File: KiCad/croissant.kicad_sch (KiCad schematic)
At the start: 7 parts, among them J1 USB_C_Receptacle, U1 LMC555xM

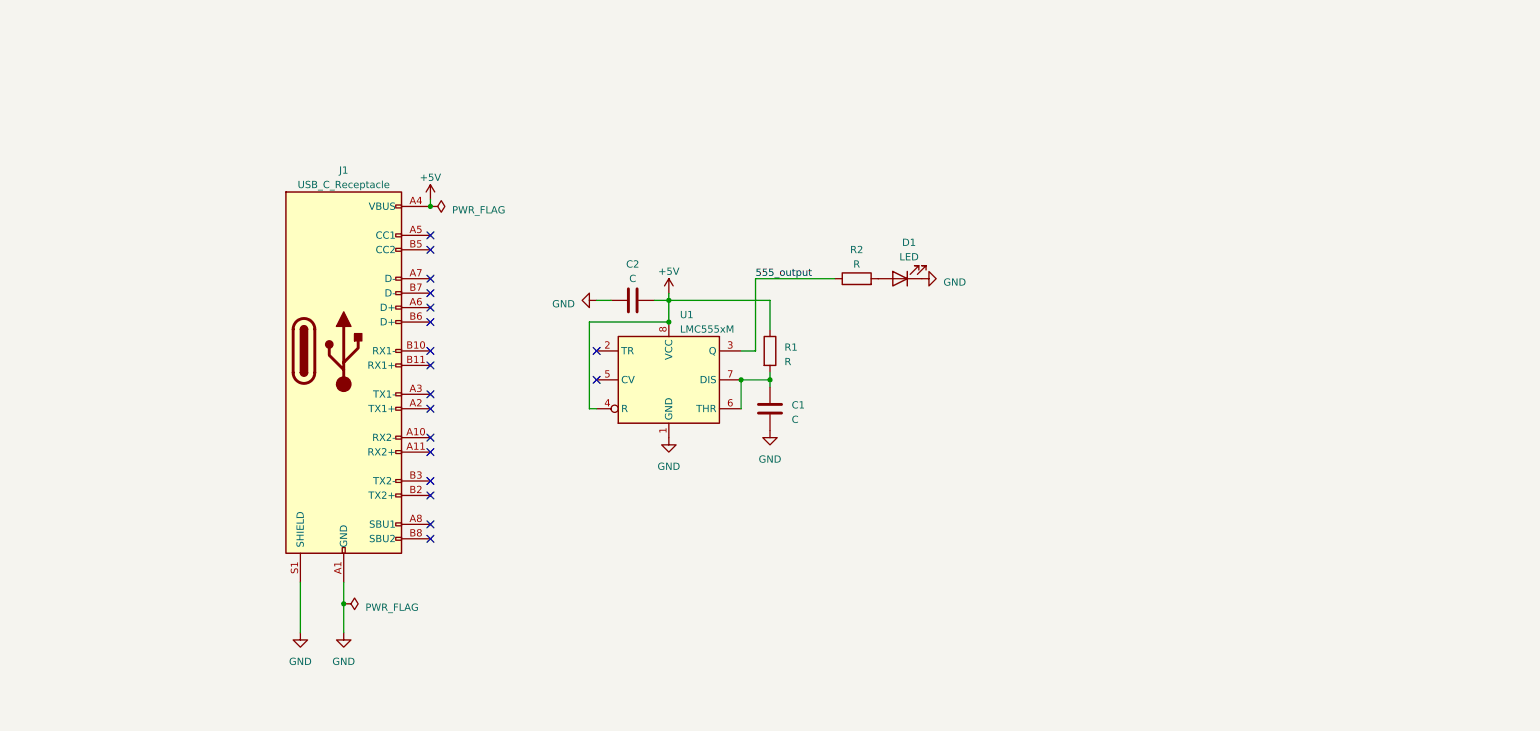
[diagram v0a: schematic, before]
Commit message: Add Kicad schematic
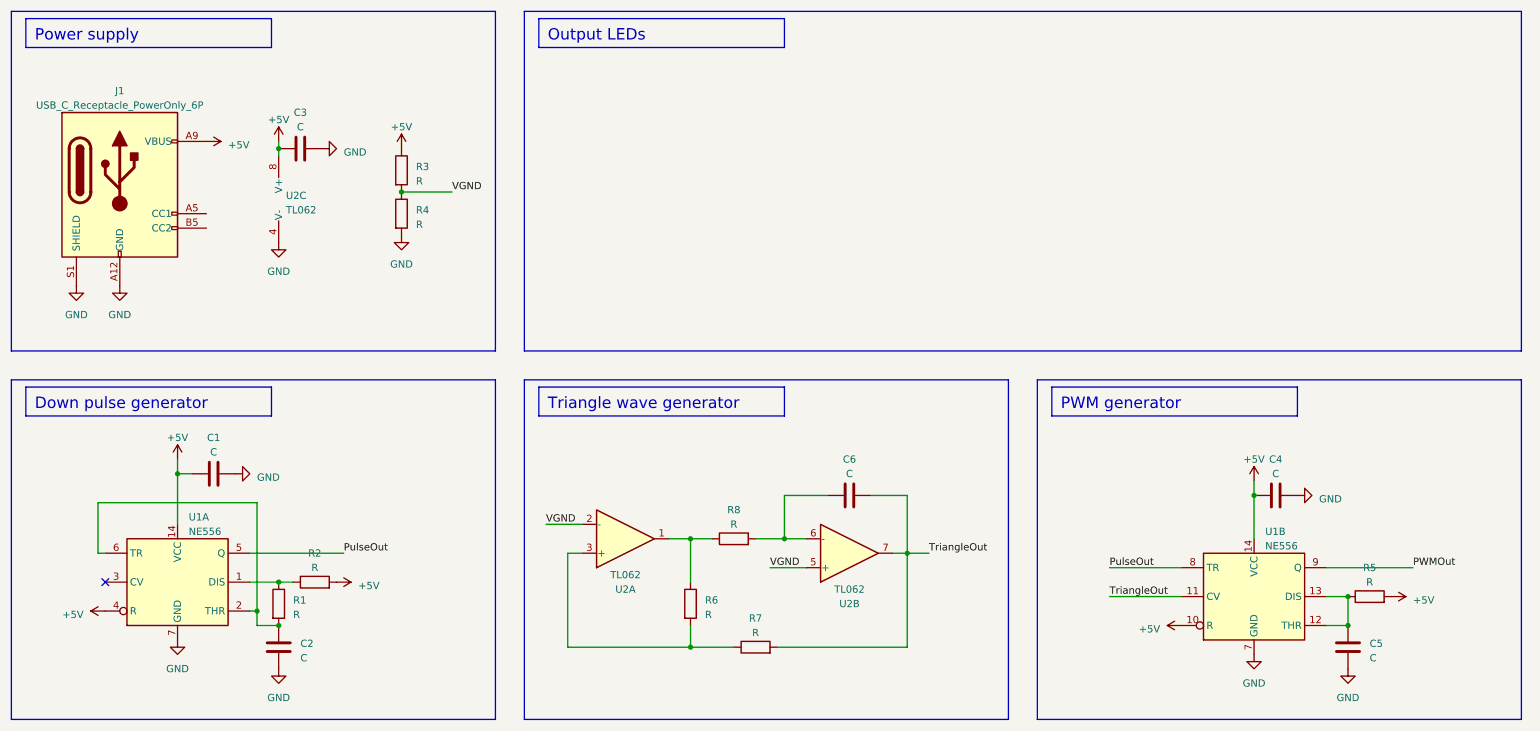
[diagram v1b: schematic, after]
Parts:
- removed D1: LED, LED_SMD:LED_0603_1608Metric, symbol Device:LED
- removed J1: USB_C_Receptacle, Connector_USB:USB_C_Receptacle_Molex_105450-0101, symbol Connector:USB_C_Receptacle
- removed U1: LMC555xM, Package_SO:SOIC-8_3.9x4.9mm_P1.27mm, symbol Timer:LMC555xM
- added C3, C4, C5, C6: C, symbol Device:C
- added J1: USB_C_Receptacle_PowerOnly_6P, symbol Connector:USB_C_Receptacle_PowerOnly_6P
- added R3, R4, R5, R6, R7, R8: R, symbol Device:R
- added U1: NE556, symbol Timer:NE556
- added U2: TL062, symbol Amplifier_Operational:TL062
- C1, C2: footprint Capacitor_SMD:C_0805_2012Metric -> (none)
- R1, R2: footprint Resistor_SMD:R_1210_3225Metric -> (none)
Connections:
- net +5V: now also C1.1, R2.2, C3.1, C4.1, J1.A9 (VBUS), J1.B9 (VBUS), R3.1, R5.2, U1.10 (R), U1.14 (VCC), U1.14 (VCC), U1.4 (R), U2.8 (V+); no longer C2.2, R1.1
- net GND: now also C3.2, C4.2, C5.1, J1.A12 (GND), J1.B12 (GND), J1.S1 (SHIELD), R4.2, U1.7 (GND), U1.7 (GND), U2.4 (V-)
- net at R1.2: now also C2.2, U1.2 (THR), U1.6 (TR); no longer C1.1
- net 555_output: no longer names the net of R2.1
- net 555_output: now also R1.1, U1.1 (DIS)
- new net: R6.2, R7.1, U2.3 (+)
- new net: C6.1, R8.2, U2.6 (-)
- new net: C5.2, R5.1, U1.12 (THR), U1.13 (DIS)
- new net: R6.1, R8.1, U2.1
- new net PWMOut: U1.9 (Q)
- new net PulseOut: U1.5 (Q), U1.8 (TR)
- new net TriangleOut: C6.2, R7.2, U1.11 (CV), U2.7
- new net VGND: R3.2, R4.1, U2.2 (-), U2.5 (+)
- no-connect marks 18 -> 1

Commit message: Add board outline
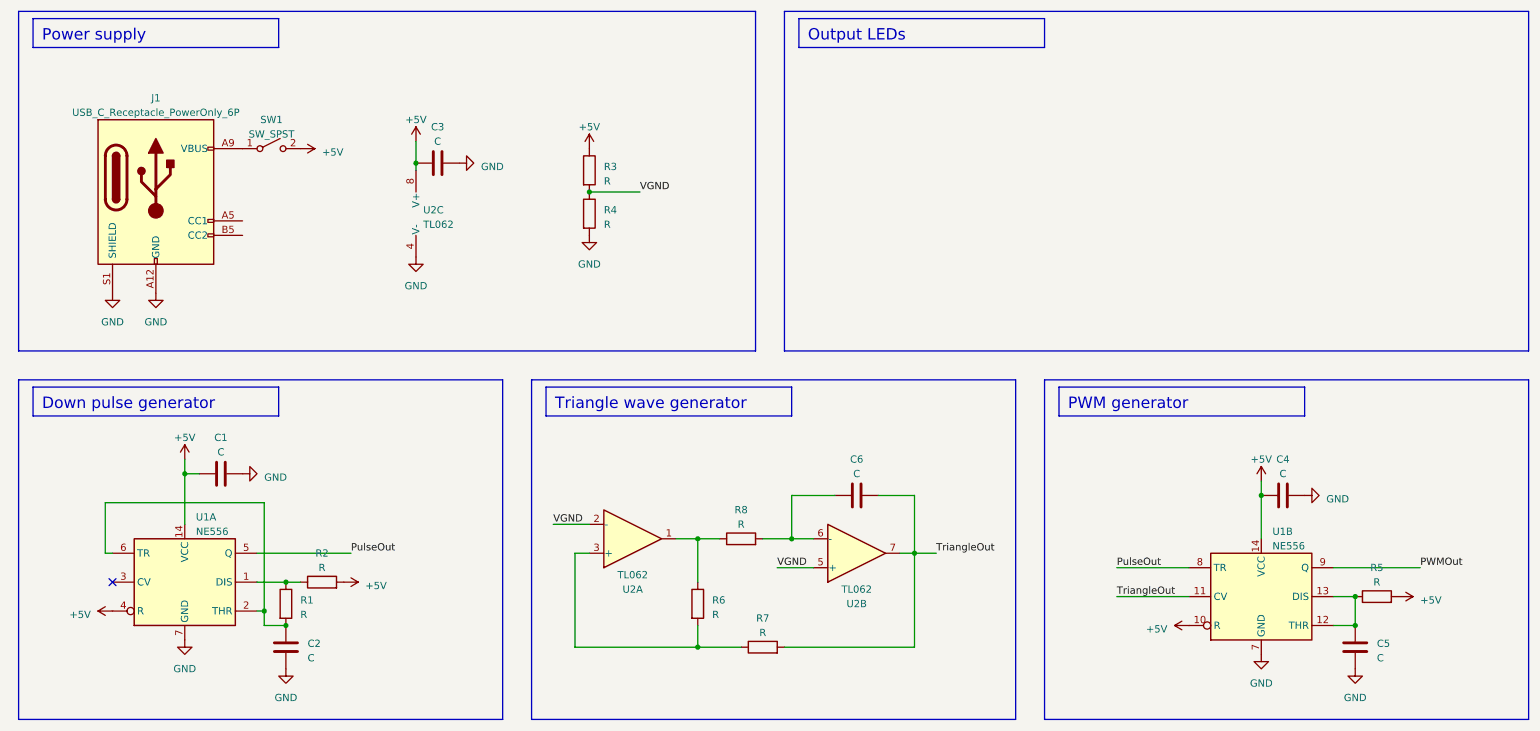
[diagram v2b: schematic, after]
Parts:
- added SW1: SW_SPST, symbol Switch:SW_SPST
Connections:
- net +5V: now also SW1.2 (B); no longer J1.A9 (VBUS), J1.B9 (VBUS)
- new net: J1.A9 (VBUS), J1.B9 (VBUS), SW1.1 (A)
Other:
- moved on the sheet: C1, C2, C3, C4, C5, C6, J1, R1, R2, R3, R4, R5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

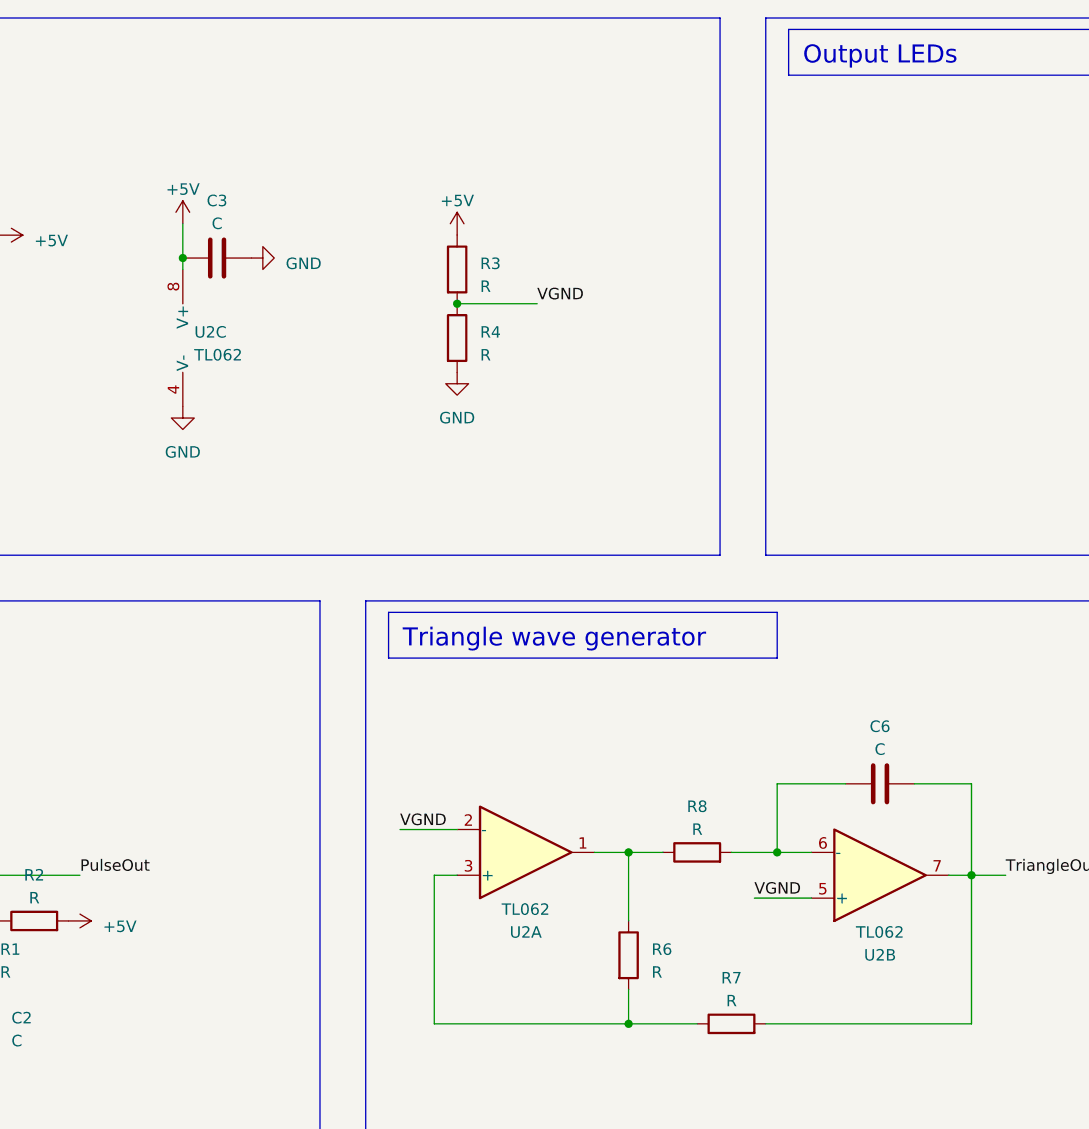
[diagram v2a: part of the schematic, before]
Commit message: Switch to TL064
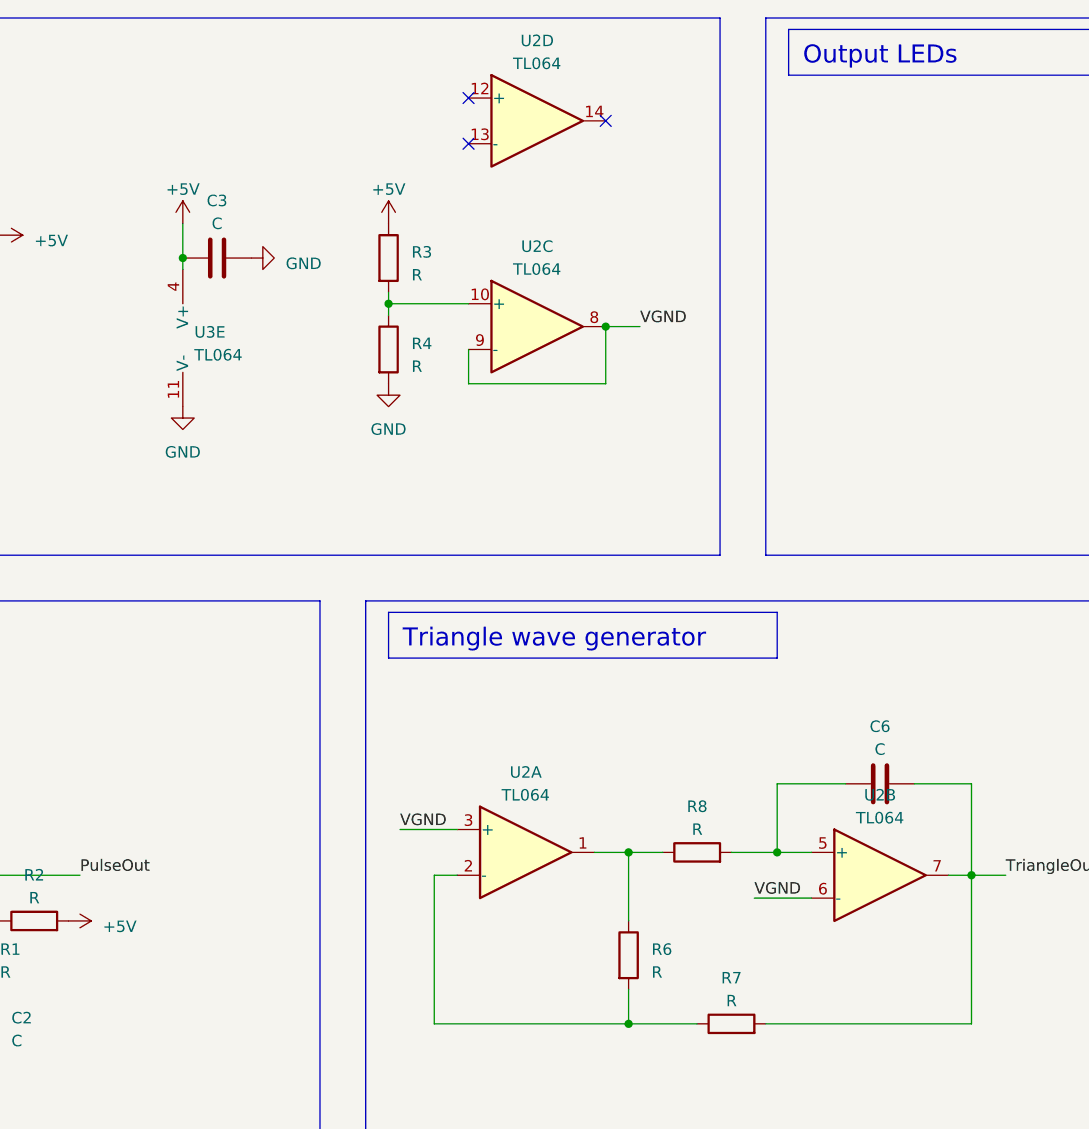
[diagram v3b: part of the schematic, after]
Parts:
- removed U2: TL062, symbol Amplifier_Operational:TL062
- added U2, U3: TL064, symbol Amplifier_Operational:TL064
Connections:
- net +5V: now also U3.4 (V+)
- net GND: now also U3.11 (V-)
- net TriangleOut: now also U2.7
- net VGND: now also U2.3 (+), U2.6 (-), U2.8, U2.9 (-); no longer R3.2, R4.1
- net at R6.2, R7.1: now also U2.2 (-)
- net at C6.1, R8.2: now also U2.5 (+)
- net at R6.1, R8.1: now also U2.1
- new net: R3.2, R4.1, U2.10 (+)
- no-connect marks 1 -> 4
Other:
- moved on the sheet: R3, R4

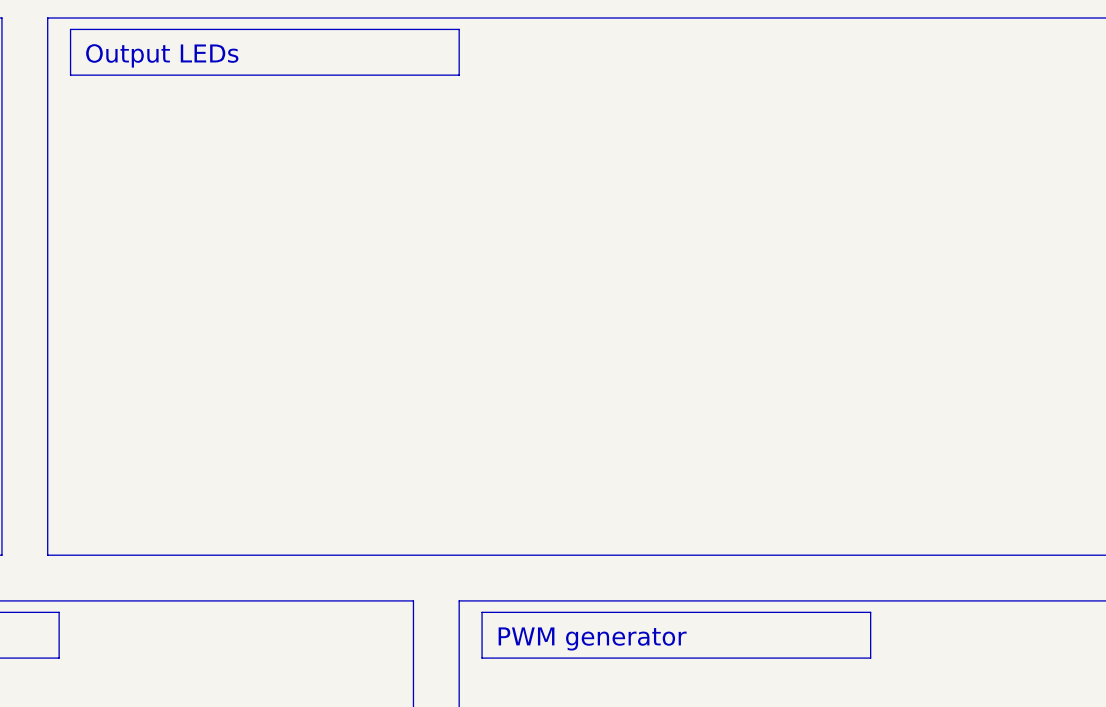
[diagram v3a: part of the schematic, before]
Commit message: Add LEDs
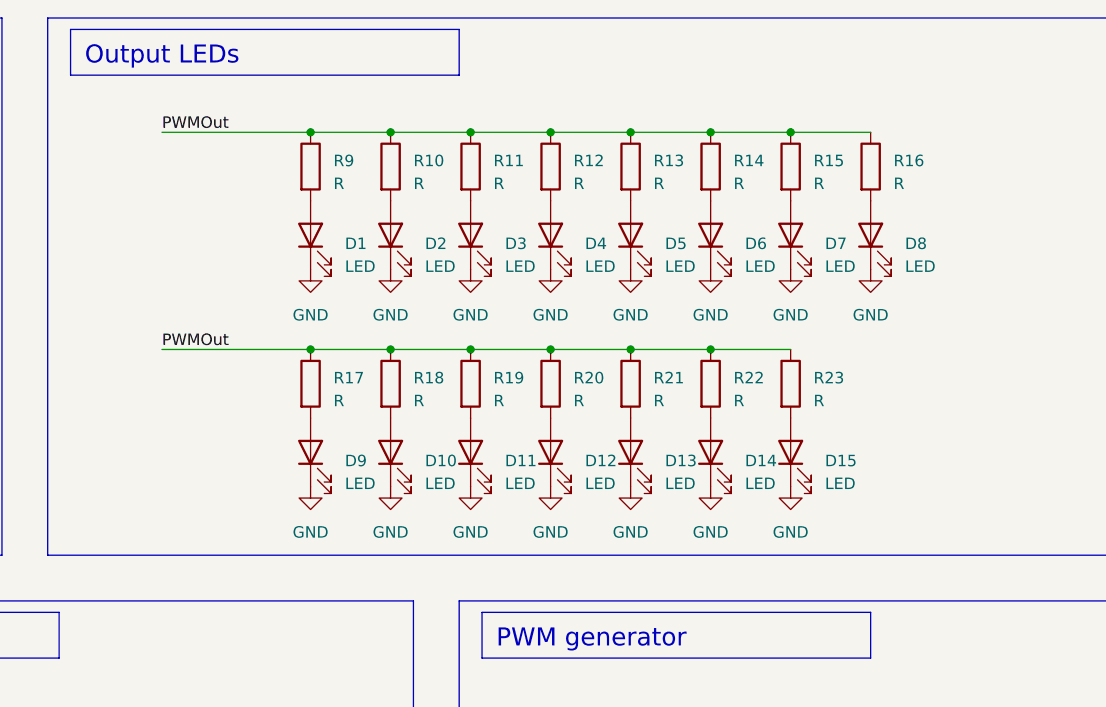
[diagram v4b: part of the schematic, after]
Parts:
- added D1, D10, D11, D12, D13, D14, D15, D2, D3, D4, D5, D6, D7, D8, D9: LED, symbol Device:LED
- added R10, R11, R12, R13, R14, R15, R16, R17, R18, R19, R20, R21, R22, R23, R9: R, symbol Device:R
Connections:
- net GND: now also D1.1 (K), D10.1 (K), D11.1 (K), D12.1 (K), D13.1 (K), D14.1 (K), D15.1 (K), D2.1 (K), D3.1 (K), D4.1 (K), D5.1 (K), D6.1 (K), D7.1 (K), D8.1 (K), D9.1 (K)
- net PWMOut: now also R10.1, R11.1, R12.1, R13.1, R14.1, R15.1, R16.1, R17.1, R18.1, R19.1, R20.1, R21.1, R22.1, R23.1, R9.1
- new net: D1.2 (A), R9.2
- new net: D7.2 (A), R15.2
- new net: D13.2 (A), R21.2
- new net: D5.2 (A), R13.2
- new net: D8.2 (A), R16.2
- new net: D3.2 (A), R11.2
- new net: D6.2 (A), R14.2
- new net: D4.2 (A), R12.2
- new net: D9.2 (A), R17.2
- new net: D15.2 (A), R23.2
- new net: D12.2 (A), R20.2
- new net: D11.2 (A), R19.2
- new net: D14.2 (A), R22.2
- new net: D2.2 (A), R10.2
- new net: D10.2 (A), R18.2

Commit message: Fix opamp orientation
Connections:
- net VGND: now also U2.2 (-), U2.5 (+); no longer U2.3 (+), U2.6 (-)
- net at C6.1, R8.2: now also U2.6 (-); no longer U2.5 (+)
- net at R6.2, R7.1: now also U2.3 (+); no longer U2.2 (-)
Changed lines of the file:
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@@
     (effects (font (size 1.27 1.27)) (justify left bottom))
   )
-  (symbol (lib_id "Amplifier_Operational:TL064") (at 163.83 127 0) (unit 2)
-    (in_bom yes) (on_board yes) (dnp no) (fields_autoplaced)
-    (property "Reference" "U2" (at 163.83 118.11 0)
-      (effects (font (size 1.27 1.27)))
-    )
-    (property "Value" "TL064" (at 163.83 120.65 0)
-      (effects (font (size 1.27 1.27)))
-    )
-    (property "Footprint" "" (at 162.56 124.46 0)
-      (effects (font (size 1.27 1.27)) hide)
-    )
-    (property "Datasheet" "http://www.ti.com/lit/ds/symlink/tl061.pdf" (at 165.1 121.92 0)
+  (symbol (lib_id "Amplifier_Operational:TL064") (at 163.83 127 0) (mirror x) (unit 2)
+    (in_bom yes) (on_board yes) (dnp no)
+    (property "Reference" "U2" (at 163.83 135.89 0)
+      (effects (font (size 1.27 1.27)))
+    )
+    (property "Value" "TL064" (at 163.83 133.35 0)
+      (effects (font (size 1.27 1.27)))
+    )
+    (property "Footprint" "" (at 162.56 129.54 0)
+      (effects (font (size 1.27 1.27)) hide)
+    )
+    (property "Datasheet" "http://www.ti.com/lit/ds/symlink/tl061.pdf" (at 165.1 132.08 0)
       (effects (font (size 1.27 1.27)) hide)
     )
@@
     )
   )
-  (symbol (lib_id "Amplifier_Operational:TL064") (at 124.46 124.46 0) (unit 1)
-    (in_bom yes) (on_board yes) (dnp no) (fields_autoplaced)
-    (property "Reference" "U2" (at 124.46 115.57 0)
-      (effects (font (size 1.27 1.27)))
-    )
-    (property "Value" "TL064" (at 124.46 118.11 0)
-      (effects (font (size 1.27 1.27)))
-    )
-    (property "Footprint" "" (at 123.19 121.92 0)
-      (effects (font (size 1.27 1.27)) hide)
-    )
-    (property "Datasheet" "http://www.ti.com/lit/ds/symlink/tl061.pdf" (at 125.73 119.38 0)
-      (effects (font (size 1.27 1.27)) hide)
-    )
+  (symbol (lib_id "Amplifier_Operational:TL064") (at 124.46 124.46 0) (mirror x) (unit 1)
+    (in_bom yes) (on_board yes) (dnp no)
+    (property "Reference" "U2" (at 124.46 133.35 0)
+      (effects (font (size 1.27 1.27)))
+    )
+    (property "Value" "TL064" (at 124.46 130.81 0)
+      (effects (font (size 1.27 1.27)))
+    )
+    (property "Footprint" "" (at 123.19 127 0)
+      (effects (font (size 1.27 1.27)) hide)
+    )
+    (property "Datasheet" "http://www.ti.com/lit/ds/symlink/tl061.pdf" (at 125.73 129.54 0)
+      (effects (font (size 1.27 1.27)) hide)
+    )

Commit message: Add LED driving transistor
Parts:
- added C7: C, symbol Device:C
- added Q1: NMOS, symbol Simulation_SPICE:NMOS
- added R24: 0, symbol Device:R
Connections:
- net +5V: now also R10.1, R11.1, R12.1, R13.1, R14.1, R15.1, R16.1, R17.1, R18.1, R19.1, R20.1, R21.1, R22.1, R23.1, R9.1, C7.1, Q1.1 (D), R24.1
- net GND: now also C7.2, Q1.3 (S)
- removed net PWMOut: R10.1, R11.1, R12.1, R13.1, R14.1, R15.1, R16.1, R17.1, R18.1, R19.1, R20.1, R21.1, R22.1, R23.1, R9.1, U1.9 (Q)
- new net: Q1.2 (G), R24.2, U1.9 (Q)
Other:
- moved on the sheet: C4, C5, R5, U1B
